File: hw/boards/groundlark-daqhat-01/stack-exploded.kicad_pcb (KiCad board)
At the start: 8 copper layers, 85 x 56 mm, 140 parts, among them J1 Raspberry Pi 40-pin, J4 FPGA test UART/reset, J80 LSHM-150-04.0-L-DV-A-S-K-TR, J81 LSHM-150-04.0-L-DV-A-S-K-TR, J82 LSHM-130-04.0-L-DV-A-S-K-TR, J83 1715721, J90 GEO + / - / SHIELD, Q1 2N7002, U1 24LC32A, U100 TMUX1574PWR, U101 TMUX1574PWR, U102 TCA9534PWR, U103 SN74LVC1G10DCKR, U104 TLV809EA30DBZR, U105 TLV809EA30DBZR, U11 LSM6DSOTR, U12 LSM6DSOTR, U13 LSM6DSOTR, U14 LSM6DSOTR, U20 SCL3300-D01, U22 ADS122C04, U40 TLV1117LV33DCYR, U41 SN74LVC8T245PWR, U42 SN74LVC8T245PWR, U43 ISO1640BDR, U51 TXU0202DCUR, U52 TLV803EA30DBZR

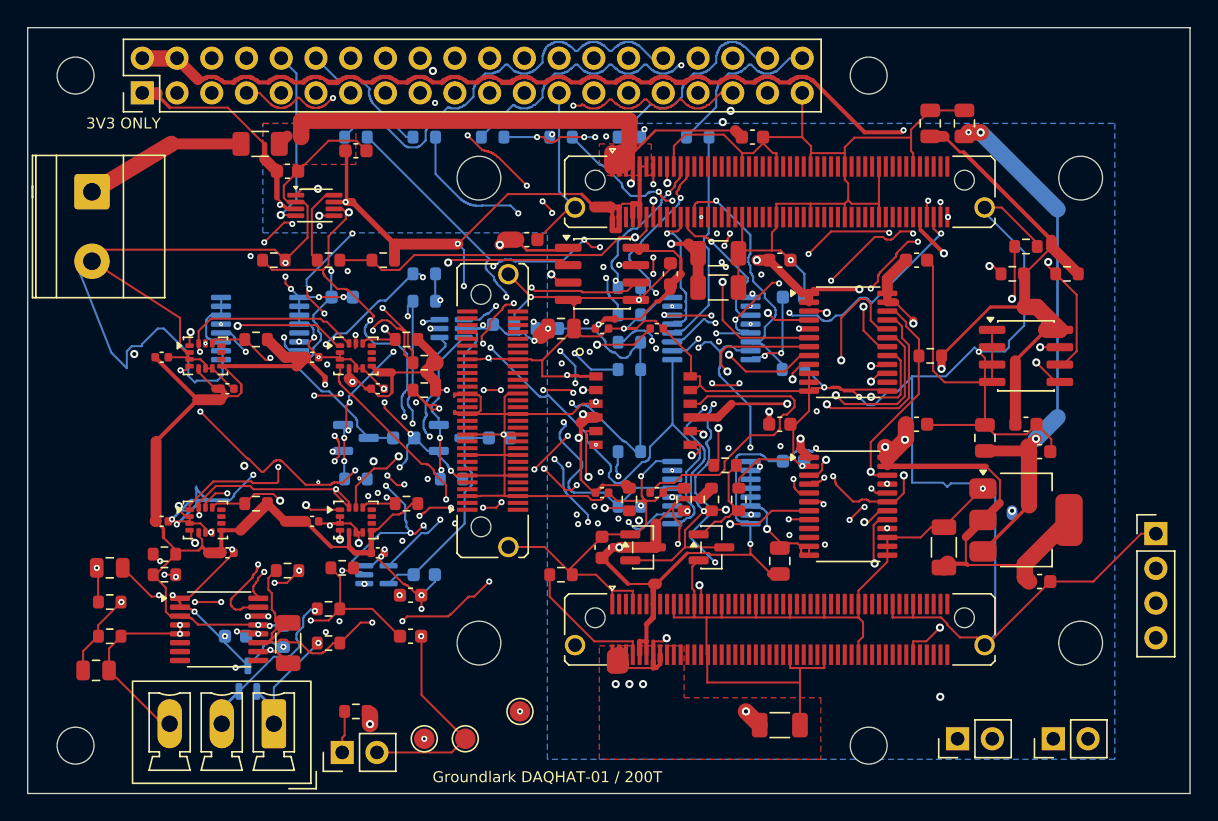
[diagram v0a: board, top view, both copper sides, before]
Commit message: Harden DAQHAT-01 assembly exports and refresh stack overview
Publish the current three-IMU six-layer revision and matching software. Capture exact-part sourcing, shortage substitutions and numbered-pad rotation mappings with regression and full/overlay integration tests. Preserve validated BOM bytes across Git checkouts. Replace README images with the current stack and a dimensioned geophone illustration; keep fabrication packages local.
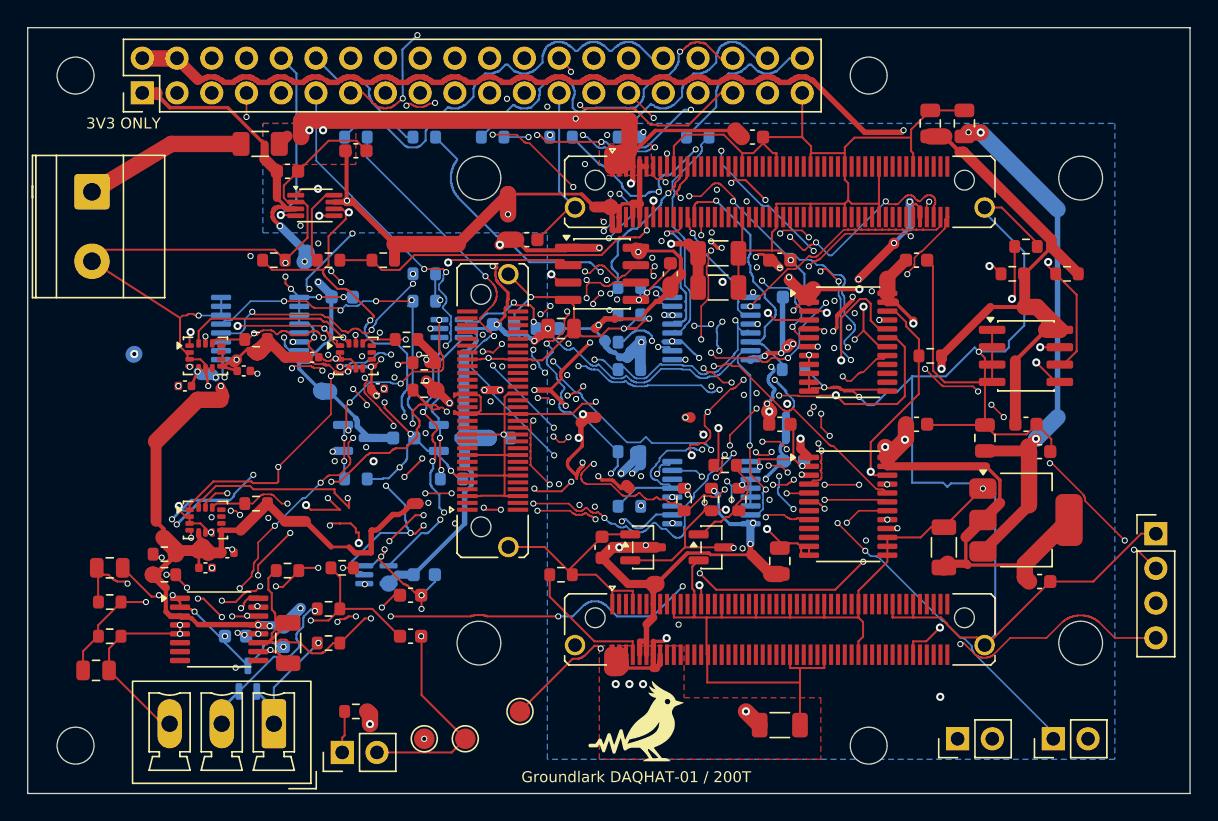
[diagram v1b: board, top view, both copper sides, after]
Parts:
- removed C18, C19, C20, C21, C22, C23: 100n, Groundlark:Capacitor_SMD__C_0402_1005Metric
- removed R14, R20: 10k, Groundlark:Resistor_SMD__R_0603_1608Metric
- removed U14: LSM6DSOTR, Groundlark:Package_LGA__LGA-14_3x2.5mm_P0.5mm_LayoutBorder3x4y
- removed U20: SCL3300-D01, Groundlark:Groundlark__SCL3300_D01
- C106: value (none) -> 100n
- U106: value (none) -> SN74LVC1G08DCKR
- moved C16 4.67 mm to (63.0, 89.5)
- moved C12 2.70 mm to (61.5, 76.2), turned to 180 degrees
- moved C13 1.77 mm to (65.8, 75.1)
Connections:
- J1 pad 18: PI_IMU4_INT -> 18
- J1 pad 31: PI_IMU4_CS -> 31
- J1 pad 33: PI_TILT_CS -> 33
- J80 pad 18: 18 -> j80-18
- J81 pad 31: 31 -> j81-31
- J81 pad 33: 33 -> j81-33
- U41 pad 15: TILT_CS -> u41-15
- U41 pad 16: IMU4_CS -> u41-16
- U41 pad 8: PI_IMU4_CS -> GND
- U41 pad 9: PI_TILT_CS -> GND
- U42 pad 17: IMU4_INT -> GND
- U42 pad 7: PI_IMU4_INT -> u42-7
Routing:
- net GND: track 781.2 -> 654.3 mm, vias 55 -> 67
- net PI_IMU4_INT: track 64.3 -> 0.00 mm, vias 2 -> 0
- net IMU4_CS: track 51.5 -> 0.00 mm, vias 3 -> 0
- net FPGA_3V3: track 259.0 -> 208.9 mm, vias 21 -> 27
- net IMU4_INT: track 46.6 -> 0.00 mm, vias 2 -> 0
- net TILT_CS: track 34.3 -> 0.00 mm, vias 3 -> 0
- net PI_TILT_CS: track 30.1 -> 0.00 mm, vias 2 -> 0
- net PI_IMU1_INT: track 48.4 -> 78.2 mm, vias 1 -> 10
- net PI_IMU4_CS: track 28.7 -> 0.00 mm, vias 1 -> 0
- net TILT_DEXT: track 22.4 -> 0.00 mm
- net FPGA_RESET_GPIO: track 70.8 -> 52.0 mm, vias 3 -> 6
- net LINK_DQ2: track 28.1 -> 42.8 mm, vias 4 -> 7
- net FPGA_VIN: track 106.7 -> 119.8 mm, vias 7 -> 12
- net SPI_MISO: track 108.2 -> 95.9 mm, vias 12 -> 20
- net I2C_SDA: track 59.3 -> 47.1 mm, vias 7 -> 12
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- added copper zone on In1.Cu, net GND
- added copper zone on In4.Cu, net GND
- removed copper zone on In2.Cu, net GND
- removed copper zone on In5.Cu, net GND
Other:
- copper layers 8 -> 6
